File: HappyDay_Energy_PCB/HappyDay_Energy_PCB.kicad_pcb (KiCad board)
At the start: 2 copper layers, 78 parts, among them J1 Conn_01x03, J10 GS3, J11 GS3, J17 GS3, J18 GS3, J2 TRS3.5Female, J3 TRS3.5Female, M1 ATM90E26_ATM90E26, M2 ATM90E26_ATM90E26, U1 120VAC->3.3VDC REG, U2 dc-dc, U3 Si865, U4 FeatherHuzzah, Y1 Crystal_Small, Y2 Crystal_Small

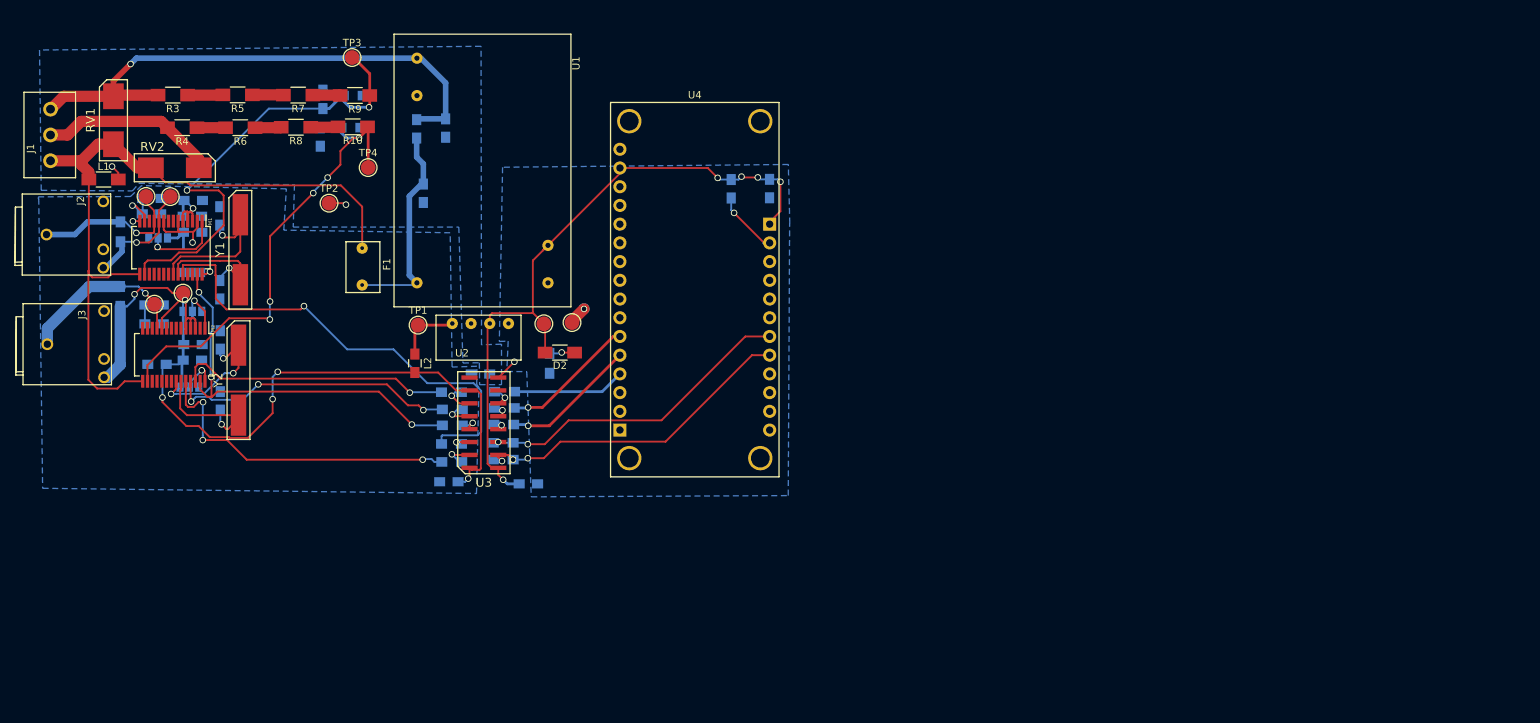
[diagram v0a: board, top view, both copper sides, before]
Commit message: Kicad PCB sent to OSH Park
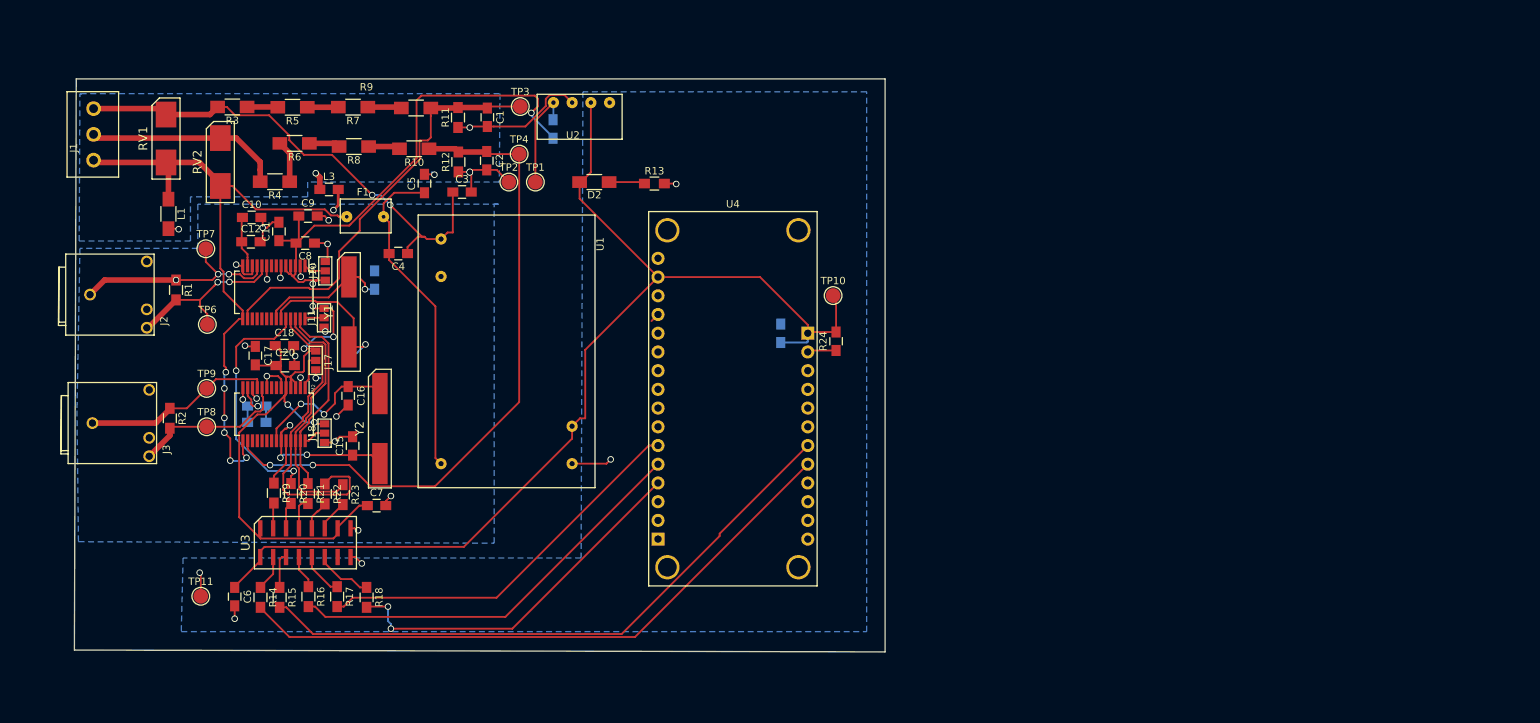
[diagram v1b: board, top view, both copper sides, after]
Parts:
- C1, C10, C11, C12, C15, C16, C17, C18, C2, C20, C3, C4, C5, C6, C7, C8, C9, J10, J11, J17, J18, L3, R1, R11, R12, R13, R14, R15, R16, R17, R18, R19, R2, R20, R21, R22, R23, R24: moved to F.Cu
- L2: moved to B.Cu
- moved TP11 62.6 mm to (92.4, 135.2)
- moved C6 42.7 mm to (97.0, 135.2), turned to 270 degrees
- moved TP10 39.4 mm to (178.2, 94.4)
- moved R14 37.9 mm to (100.5, 135.3), turned to 270 degrees
- moved L2 36.9 mm to (140.2, 71.8)
- moved R15 36.9 mm to (103.1, 135.3), turned to 270 degrees
- moved R16 35.3 mm to (107.0, 135.2), turned to 270 degrees
- moved R17 34.2 mm to (110.9, 135.2), turned to 270 degrees
- moved R18 33.6 mm to (114.9, 135.3), turned to 270 degrees
- moved U2 33.0 mm to (146.6, 71.0)
- moved L3 32.4 mm to (109.8, 80.0), turned to 0 degrees
- moved U3 29.2 mm to (106.6, 127.9), turned to 0 degrees
- moved R13 28.2 mm to (153.9, 79.2), turned to 0 degrees
- moved R24 25.1 mm to (178.6, 100.6)
- moved TP1 25.1 mm to (137.8, 79.0)
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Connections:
- net /ATM90_Circuit/SCK_MCU renamed /ATM90_Circuit/SCK
- R14 pad 1: CS1_MCU -> /ATM90_Circuit/CS1
- R15 pad 1: CS0_MCU -> /ATM90_Circuit/CS0
- R16 pad 1: MOSI_MCU -> /ATM90_Circuit/MOSI
- R18 pad 1: MISO_MCU -> /ATM90_Circuit/MISO
- U3 pad 2: CS1_MCU -> /ATM90_Circuit/CS1
- U3 pad 3: CS0_MCU -> /ATM90_Circuit/CS0
- U3 pad 4: MOSI_MCU -> /ATM90_Circuit/MOSI
- U3 pad 6: MISO_MCU -> /ATM90_Circuit/MISO
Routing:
- net 3.3V_MCU: track 94.2 -> 149.0 mm, vias 5 -> 0
- net +3.3VA: track 111.3 -> 159.5 mm, vias 5 -> 7
- net CS0_MCU: track 43.0 -> 83.9 mm, vias 2 -> 0
- net CS1_MCU: track 45.4 -> 85.7 mm, vias 3 -> 0
- net GNDD: track 11.1 -> 49.9 mm, vias 2 -> 19
- net CS1_ATM: track 44.8 -> 6.43 mm, vias 3 -> 0
- net MOSI_MCU: track 20.6 -> 56.6 mm, vias 3 -> 0
- net SCLK_MCU: track 18.4 -> 52.6 mm, vias 1 -> 0
- net MISO_MCU: track 18.3 -> 50.7 mm, vias 1 -> 2
- net CS0_ATM: track 64.0 -> 33.0 mm, vias 1 -> 2
- net GNDA: track 4.49 -> 34.7 mm, vias 2 -> 6
- net MOSI_ATM: track 54.3 -> 26.9 mm, vias 3 -> 0
- net L1_SAMP: track 65.4 -> 91.0 mm, vias 5 -> 2
- net Net-(C4-Pad2): track 28.9 -> 44.7 mm
- net N: track 98.6 -> 88.1 mm, vias 0 -> 6
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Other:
- board outline added: 110 x 77.8 mm

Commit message: updates, particularly to layout - but not finished
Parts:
- added C23: .33u, Capacitors_SMD:C_0805, B.Cu at (176.6, 78.4)
- added C24: .33u, Capacitors_SMD:C_0805, B.Cu at (170.3, 78.3)
- added C25: .33u, Capacitors_SMD:C_0805, B.Cu at (171.0, 93.0)
- added C26: .33u, Capacitors_SMD:C_0805, B.Cu at (174.5, 93.0)
- added R25: 100, Capacitors_SMD:C_0805, B.Cu at (173.7, 78.4)
- added R26: 100, Capacitors_SMD:C_0805, B.Cu at (167.7, 78.2)
- added R27: 100, Capacitors_SMD:C_0805, B.Cu at (167.6, 93.0)
- added R28: 100, Capacitors_SMD:C_0805, B.Cu at (177.8, 93.0)
- C1, C10, C11, C12, C17, C18, C2, C20, C5, C6, C7, C8, C9, L3: footprint Capacitors_SMD:C_0805_HandSoldering -> Capacitors_SMD:C_0805
- C13, C14: value 18p -> 27p; footprint Capacitors_SMD:C_0805_HandSoldering -> Capacitors_SMD:C_0805; moved to F.Cu
- C15: value 18p -> 27p; footprint Capacitors_SMD:C_0805_HandSoldering -> Capacitors_SMD:C_0805; moved to B.Cu
- C16: value 18p -> 27p; footprint Capacitors_SMD:C_0805_HandSoldering -> Capacitors_SMD:C_0805
- C19, C21, C22, L2: footprint Capacitors_SMD:C_0805_HandSoldering -> Capacitors_SMD:C_0805; moved to F.Cu
- C3, C4, R24: footprint Capacitors_SMD:C_0805_HandSoldering -> Capacitors_SMD:C_0805; moved to B.Cu
- D2: value LED -> IND_LED
- J10, J11, U3: moved to B.Cu
- L1: footprint Capacitors_SMD:C_1206_HandSoldering -> Capacitors_SMD:C_1206
- R1, R14, R15, R16, R17, R18, R19, R2, R20, R21, R22, R23: footprint Resistors_SMD:R_0805_HandSoldering -> Capacitors_SMD:C_0805; moved to B.Cu
- R10: footprint Resistors_SMD:R_1206_HandSoldering -> Capacitors_SMD:C_1206
- R11, R12: footprint Resistors_SMD:R_0805_HandSoldering -> Capacitors_SMD:C_0805
- R13: value 330 -> 499; footprint Resistors_SMD:R_0805_HandSoldering -> Capacitors_SMD:C_0805; moved to B.Cu
- R3, R4, R5, R6, R7, R8, R9: footprint Resistors_SMD:R_1206_HandSoldering -> Capacitors_SMD:C_1206; moved to B.Cu
- U1: value 120VAC->3.3VDC REG -> RAC03-3.3SGA
- moved C19 174.5 mm to (267.2, 61.9), turned to 90 degrees
- moved C17 172.9 mm to (269.6, 69.5)
- moved C21 170.4 mm to (263.7, 61.9), turned to 90 degrees
- moved C18 165.7 mm to (266.4, 69.4), turned to 90 degrees
- moved C20 163.0 mm to (263.1, 69.3), turned to 90 degrees
- moved M2 159.8 mm to (256.2, 67.5), turned to 180 degrees
- moved J17 156.6 mm to (258.3, 59.3), turned to 0 degrees
- moved J18 153.3 mm to (252.8, 59.3)
- moved R14 150.8 mm to (246.0, 95.7)
- moved C15 150.6 mm to (255.9, 67.3), turned to 0 degrees
- moved R15 145.0 mm to (242.6, 95.8)
- moved R19 144.8 mm to (242.1, 83.4)
- moved C16 144.5 mm to (250.0, 63.9)
- moved TP9 143.7 mm to (235.2, 129.0)
- moved R20 139.8 mm to (239.2, 83.3)
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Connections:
- J2 pad 1: I1N_0 -> Net-(J2-Pad1)
- J2 pad 2: I1P_0 -> Net-(J2-Pad2)
- J3 pad 1: I1N_1 -> Net-(J3-Pad1)
- J3 pad 2: I1P_1 -> Net-(J3-Pad2)
- R1 pad 1: I1N_0 -> Net-(J2-Pad1)
- R1 pad 2: I1P_0 -> Net-(J2-Pad2)
- R2 pad 1: I1N_1 -> Net-(J3-Pad1)
- R2 pad 2: I1P_1 -> Net-(J3-Pad2)
- U1 pad 2: (no net) -> Net-(C4-Pad2)
- U1 pad 3: Net-(C4-Pad2) -> Net-(U1-Pad3)
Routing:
- net +3.3VA: track 159.5 -> 12.1 mm, vias 7 -> 0
- net 3.3V_MCU: track 149.0 -> 20.7 mm
- net CS1_MCU: track 85.7 -> 0.00 mm
- net CS0_MCU: track 83.9 -> 0.00 mm
- net MOSI_MCU: track 56.6 -> 0.00 mm
- net I1P_0: track 23.5 -> 76.8 mm, vias 2 -> 3
- net SCLK_MCU: track 52.6 -> 0.00 mm
- net MISO_MCU: track 50.7 -> 0.00 mm, vias 2 -> 0
- net GNDD: track 49.9 -> 0.00 mm, vias 19 -> 0
- net I1N_0: track 29.6 -> 66.5 mm
- net CS0_ATM: track 33.0 -> 0.00 mm, vias 2 -> 0
- net SCLK_ATM: track 43.5 -> 13.3 mm, vias 0 -> 2
- net GNDA: track 34.7 -> 8.57 mm, vias 6 -> 4
- net I1N_1: track 26.0 -> 3.42 mm
- net CLKIN_0: track 18.5 -> 0.00 mm, vias 1 -> 0
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- removed copper zone on B.Cu, net GNDD
- removed copper zone on B.Cu, net GND_MCU
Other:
- board outline removed
- net class Default: trace_width 0.254 -> 0.1524; via_dia 0.889 -> 0.6858; via_drill 0.635 -> 0.3302
- rule pad_to_mask_clearance: 0.2 -> 0
- rule via_min_drill: 0.508 -> 0.3302
- rule via_min_size: 0.889 -> 0.6858
